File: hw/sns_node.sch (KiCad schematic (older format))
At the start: 12 parts

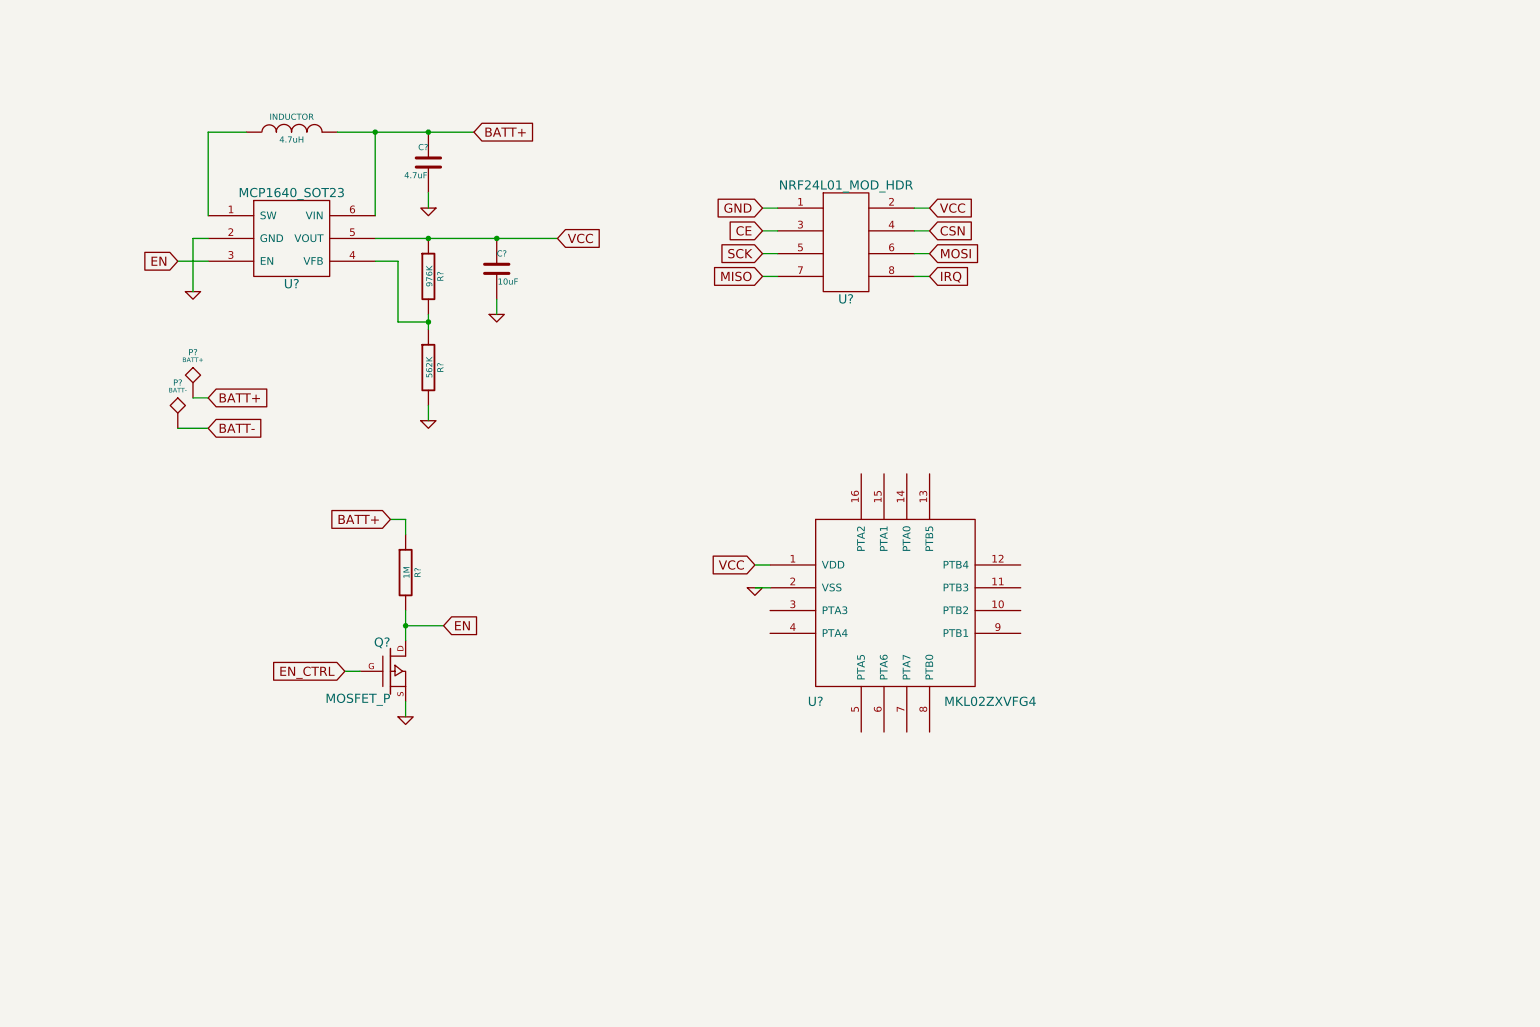
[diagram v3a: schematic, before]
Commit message: - add nrf pwr control
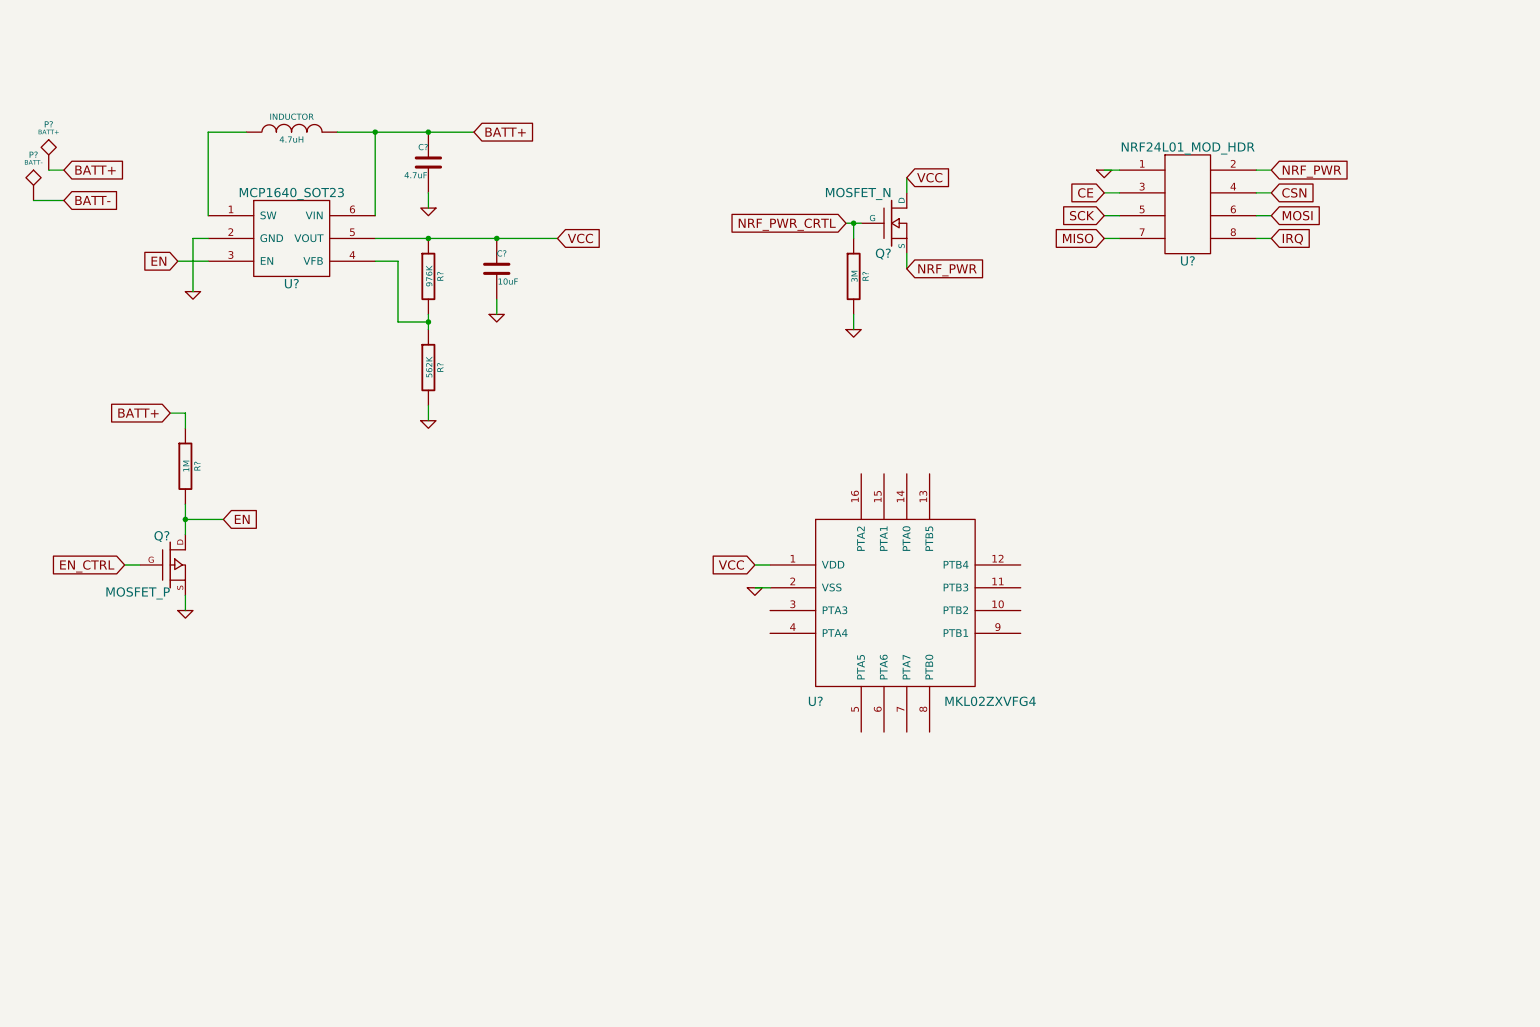
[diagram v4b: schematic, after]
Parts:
- added Q?: MOSFET_N, ~, symbol MOSFET_N
- added R?: 3M, ~, symbol R
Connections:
- net GND: now also R?.2
- net VCC: now also Q?.D; no longer U?.2
- new net NRF_PWR: Q?.S, U?.2
- new net NRF_PWR_CRTL: Q?.G, R?.1
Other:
- moved on the sheet: P?, Q?, R?, U?
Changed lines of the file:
@@
 Text GLabel 3700 1600 2    60   Input ~ 0
 BATT+
-Text GLabel 1950 3550 2    60   Input ~ 0
+Text GLabel 1000 2050 2    60   Input ~ 0
 BATT-
 $Comp
@@
 	0    -1   -1   0
 $EndComp
-Text GLabel 1950 3350 2    60   Input ~ 0
+Text GLabel 1000 1850 2    60   Input ~ 0
 BATT+
 $Comp
@@
 L TST P?
 U 1 1 5302C2B3
-P 1850 3350
-F 0 "P?" H 1850 3650 40  0000 C CNN
-F 1 "BATT+" H 1850 3600 30  0000 C CNN
-F 2 "~" H 1850 3350 60  0000 C CNN
-F 3 "~" H 1850 3350 60  0000 C CNN
-	1    1850 3350
+P 900 1850
+F 0 "P?" H 900 2150 40  0000 C CNN
+F 1 "BATT+" H 900 2100 30  0000 C CNN
+F 2 "~" H 900 1850 60  0000 C CNN
+F 3 "~" H 900 1850 60  0000 C CNN
+	1    900  1850
 	1    0    0    -1
 $EndComp
@@
 L TST P?
 U 1 1 5302C2C0
-P 1750 3550
-F 0 "P?" H 1750 3850 40  0000 C CNN
-F 1 "BATT-" H 1750 3800 30  0000 C CNN
-F 2 "~" H 1750 3550 60  0000 C CNN
-F 3 "~" H 1750 3550 60  0000 C CNN
-	1    1750 3550
-	1    0    0    -1
-$EndComp
-Wire Wire Line
-	1950 3550 1750 3550
-Wire Wire Line
-	1850 3350 1950 3350
+P 800 2050
+F 0 "P?" H 800 2350 40  0000 C CNN
+F 1 "BATT-" H 800 2300 30  0000 C CNN
+F 2 "~" H 800 2050 60  0000 C CNN
+F 3 "~" H 800 2050 60  0000 C CNN
+	1    800  2050
+	1    0    0    -1
+$EndComp
+Wire Wire Line
+	1000 2050 800  2050
+Wire Wire Line
+	900  1850 1000 1850
 Connection ~ 3050 1600
 Text GLabel 1750 2450 0    60   Input ~ 0
@@
 Wire Wire Line
 	5550 4450 5650 4450
-Text GLabel 3500 4850 2    60   Input ~ 0
+Text GLabel 2050 4150 2    60   Input ~ 0
 EN
 $Comp
 L MOSFET_P Q?
 U 1 1 5302C7F0
-P 3150 5150
-F 0 "Q?" H 3150 5340 60  0000 R CNN
-F 1 "MOSFET_P" H 3150 4970 60  0000 R CNN
-F 2 "~" H 3150 5150 60  0000 C CNN
-F 3 "~" H 3150 5150 60  0000 C CNN
-	1    3150 5150
+P 1700 4450
+F 0 "Q?" H 1700 4640 60  0000 R CNN
+F 1 "MOSFET_P" H 1700 4270 60  0000 R CNN
+F 2 "~" H 1700 4450 60  0000 C CNN
+F 3 "~" H 1700 4450 60  0000 C CNN
+	1    1700 4450
 	1    0    0    -1
 $EndComp
@@
 L R R?
 U 1 1 5302C818
-P 3250 4500
-F 0 "R?" V 3330 4500 40  0000 C CNN
-F 1 "1M" V 3257 4501 40  0000 C CNN
-F 2 "~" V 3180 4500 30  0000 C CNN
-F 3 "~" H 3250 4500 30  0000 C CNN
-	1    3250 4500
-	1    0    0    -1
-$EndComp
-Wire Wire Line
-	3500 4850 3250 4850
-Wire Wire Line
-	3250 4750 3250 4950
-Connection ~ 3250 4850
-Text GLabel 2850 5150 0    60   Input ~ 0
+P 1800 3800
+F 0 "R?" V 1880 3800 40  0000 C CNN
+F 1 "1M" V 1807 3801 40  0000 C CNN
+F 2 "~" V 1730 3800 30  0000 C CNN
+F 3 "~" H 1800 3800 30  0000 C CNN
+	1    1800 3800
+	1    0    0    -1
+$EndComp
+Wire Wire Line
+	2050 4150 1800 4150
+Wire Wire Line
+	1800 4050 1800 4250
+Connection ~ 1800 4150
+Text GLabel 1400 4450 0    60   Input ~ 0
 EN_CTRL
 Wire Wire Line
-	2950 5150 2850 5150
-Text GLabel 3150 4150 0    60   Input ~ 0
+	1500 4450 1400 4450
+Text GLabel 1700 3450 0    60   Input ~ 0
 BATT+
 Wire Wire Line
-	3150 4150 3250 4150
-Wire Wire Line
-	3250 4150 3250 4250
+	1700 3450 1800 3450
+Wire Wire Line
+	1800 3450 1800 3550
 $Comp
 L GND #PWR?
 U 1 1 5302C99C
-P 3250 5450
-F 0 "#PWR?" H 3250 5450 30  0001 C CNN
-F 1 "GND" H 3250 5380 30  0001 C CNN
-F 2 "" H 3250 5450 60  0000 C CNN
-F 3 "" H 3250 5450 60  0000 C CNN
-	1    3250 5450
-	1    0    0    -1
-$EndComp
-Wire Wire Line
-	3250 5450 3250 5350
+P 1800 4750
+F 0 "#PWR?" H 1800 4750 30  0001 C CNN
+F 1 "GND" H 1800 4680 30  0001 C CNN
+F 2 "" H 1800 4750 60  0000 C CNN
+F 3 "" H 1800 4750 60  0000 C CNN
+	1    1800 4750
+	1    0    0    -1
+$EndComp
+Wire Wire Line
+	1800 4750 1800 4650
 $Comp
 L 2X4_HDR U?
 U 1 1 53055294
-P 6150 2350
-F 0 "U?" H 6150 2000 60  0000 C CNN
-F 1 "NRF24L01_MOD_HDR" H 6150 2750 60  0000 C CNN
-F 2 "~" H 6050 2100 60  0000 C CNN
-F 3 "~" H 6050 2100 60  0000 C CNN
-	1    6150 2350
-	1    0    0    -1
-$EndComp
-Text GLabel 5600 2100 0    60   Input ~ 0
-GND
-Text GLabel 5600 2250 0    60   Input ~ 0
+P 8400 2100
+F 0 "U?" H 8400 1750 60  0000 C CNN
+F 1 "NRF24L01_MOD_HDR" H 8400 2500 60  0000 C CNN
+F 2 "~" H 8300 1850 60  0000 C CNN
+F 3 "~" H 8300 1850 60  0000 C CNN
+	1    8400 2100
+	1    0    0    -1
+$EndComp
+Text GLabel 7850 2000 0    60   Input ~ 0
 CE
-Text GLabel 5600 2400 0    60   Input ~ 0
+Text GLabel 7850 2150 0    60   Input ~ 0
 SCK
-Text GLabel 5600 2550 0    60   Input ~ 0
+Text GLabel 7850 2300 0    60   Input ~ 0
 MISO
-Text GLabel 6700 2100 2    60   Input ~ 0
+Text GLabel 8950 1850 2    60   Input ~ 0
+NRF_PWR
+Text GLabel 8950 2000 2    60   Input ~ 0
+CSN
+Text GLabel 8950 2150 2    60   Input ~ 0
+MOSI
+Text GLabel 8950 2300 2    60   Input ~ 0
+IRQ
+Wire Wire Line
+	7850 1850 7950 1850
+Wire Wire Line
+	7950 2000 7850 2000
+Wire Wire Line
+	7850 2150 7950 2150
+Wire Wire Line
+	7950 2300 7850 2300
+Wire Wire Line
+	8850 1850 8950 1850
+Wire Wire Line
+	8950 2000 8850 2000
+Wire Wire Line
+	8850 2150 8950 2150
+Wire Wire Line
+	8950 2300 8850 2300
+Text GLabel 6550 2500 2    60   Input ~ 0
+NRF_PWR
+$Comp
+L MOSFET_N Q?
+U 1 1 5305557D
+P 6450 2200
+F 0 "Q?" H 6450 2000 60  0000 R CNN
+F 1 "MOSFET_N" H 6450 2400 60  0000 R CNN
+F 2 "~" H 6450 2200 60  0000 C CNN
+F 3 "~" H 6450 2200 60  0000 C CNN
+	1    6450 2200
+	1    0    0    -1
+$EndComp
+Wire Wire Line
+	6550 1900 6550 2000
+Text GLabel 6150 2200 0    60   Input ~ 0
+NRF_PWR_CRTL
+Wire Wire Line
+	6150 2200 6250 2200
+Wire Wire Line
+	6550 2500 6550 2400
+Text GLabel 6550 1900 2    60   Input ~ 0
 VCC
-Text GLabel 6700 2250 2    60   Input ~ 0
-CSN
-Text GLabel 6700 2400 2    60   Input ~ 0
-MOSI
-Text GLabel 6700 2550 2    60   Input ~ 0
-IRQ
-Wire Wire Line
-	5600 2100 5700 2100
-Wire Wire Line
-	5700 2250 5600 2250
-Wire Wire Line
-	5600 2400 5700 2400
-Wire Wire Line
-	5700 2550 5600 2550
-Wire Wire Line
-	6600 2100 6700 2100
-Wire Wire Line
-	6700 2250 6600 2250
-Wire Wire Line
-	6600 2400 6700 2400
-Wire Wire Line
-	6700 2550 6600 2550
+$Comp
+L R R?
+U 1 1 53055831
+P 6200 2550
+F 0 "R?" V 6280 2550 40  0000 C CNN
+F 1 "3M" V 6207 2551 40  0000 C CNN
+F 2 "~" V 6130 2550 30  0000 C CNN
+F 3 "~" H 6200 2550 30  0000 C CNN
+	1    6200 2550
+	1    0    0    -1
+$EndComp
+Wire Wire Line
+	6200 2300 6200 2200
+Connection ~ 6200 2200
+$Comp
+L GND #PWR?
+U 1 1 53055869
+P 6200 2900
+F 0 "#PWR?" H 6200 2900 30  0001 C CNN
+F 1 "GND" H 6200 2830 30  0001 C CNN
+F 2 "" H 6200 2900 60  0000 C CNN
+F 3 "" H 6200 2900 60  0000 C CNN
+	1    6200 2900
+	1    0    0    -1
+$EndComp
+Wire Wire Line
+	6200 2900 6200 2800
+$Comp
+L GND #PWR?
+U 1 1 530559E5
+P 7850 1850
+F 0 "#PWR?" H 7850 1850 30  0001 C CNN
+F 1 "GND" H 7850 1780 30  0001 C CNN
+F 2 "" H 7850 1850 60  0000 C CNN
+F 3 "" H 7850 1850 60  0000 C CNN
+	1    7850 1850
+	1    0    0    -1
+$EndComp
 $EndSCHEMATC

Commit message: - add voltage sns circuit, connected to on chip comparator.
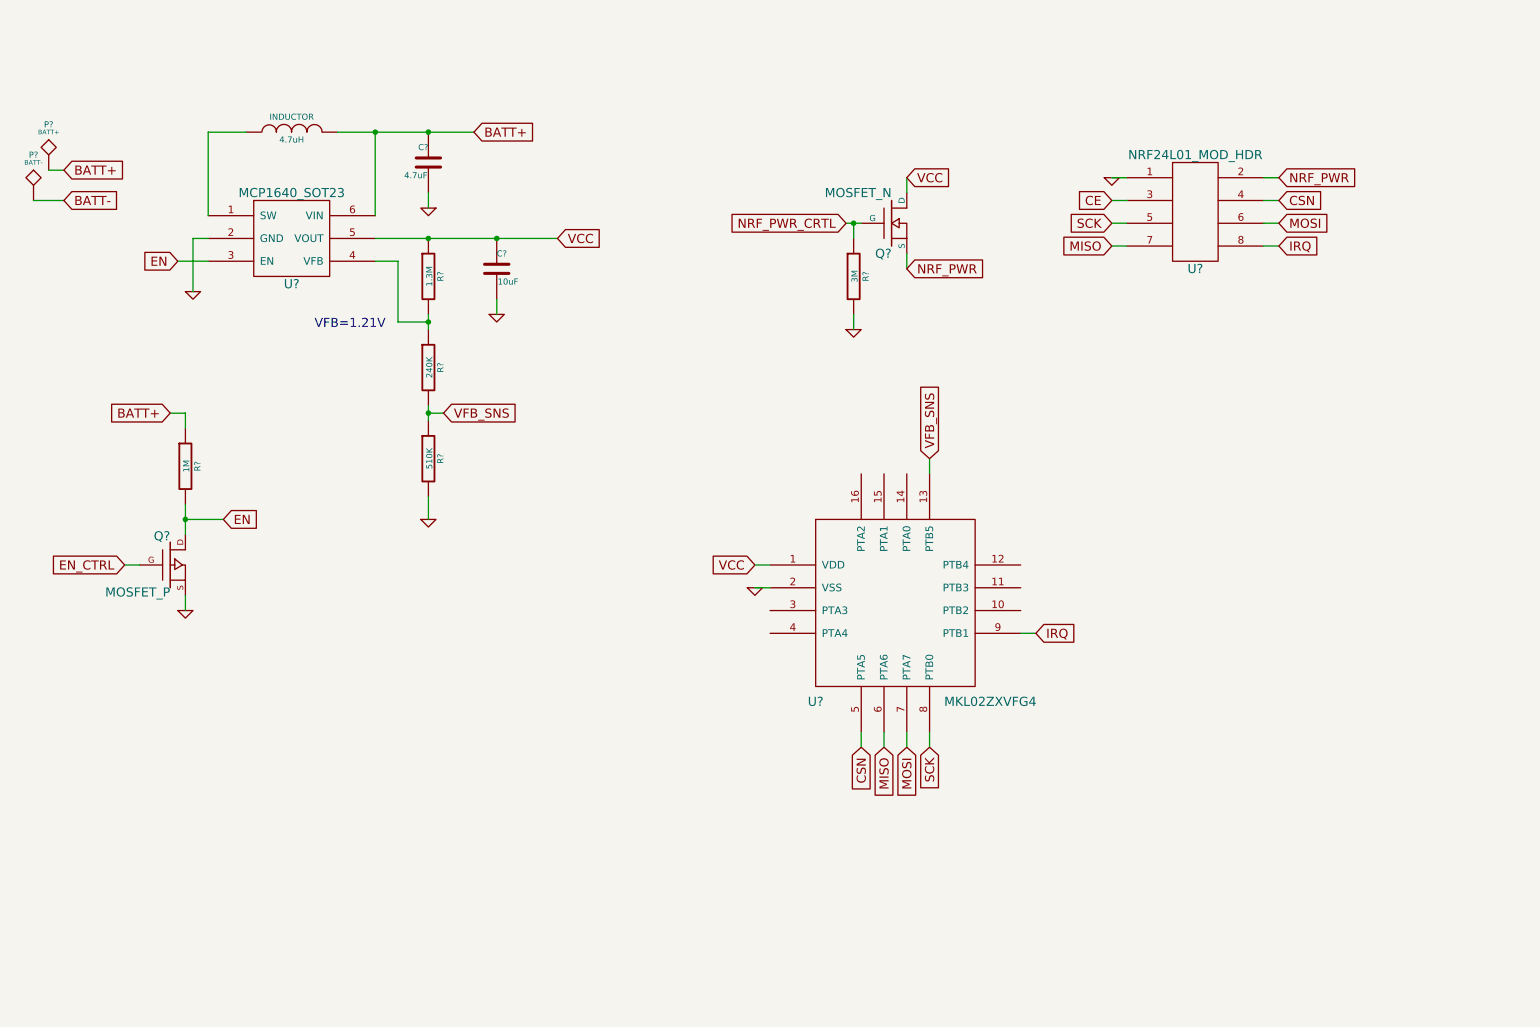
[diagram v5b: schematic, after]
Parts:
- added R?: 510K, ~, symbol R
- R?: value 976K -> 1.3M
- R?: value 562K -> 240K
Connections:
- net CSN: now also U?.5 (PTA5)
- net GND: now also R?.2; no longer R?.2
- net IRQ: now also U?.9 (PTB1)
- net MISO: now also U?.6 (PTA6)
- net MOSI: now also U?.7 (PTA7)
- net SCK: now also U?.8 (PTB0)
- net VFB_SNS: now reaches U?.13 (PTB5)
- net VFB_SNS: now also R?.2, R?.1
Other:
- note added: "VFB=1.21V"
- moved on the sheet: U?
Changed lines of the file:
@@
 P 3400 2550
 F 0 "R?" V 3480 2550 40  0000 C CNN
-F 1 "976K" V 3407 2551 40  0000 C CNN
+F 1 "1.3M" V 3407 2551 40  0000 C CNN
 F 2 "~" V 3330 2550 30  0000 C CNN
 F 3 "~" H 3400 2550 30  0000 C CNN
@@
 P 3400 3150
 F 0 "R?" V 3480 3150 40  0000 C CNN
-F 1 "562K" V 3407 3151 40  0000 C CNN
+F 1 "240K" V 3407 3151 40  0000 C CNN
 F 2 "~" V 3330 3150 30  0000 C CNN
 F 3 "~" H 3400 3150 30  0000 C CNN
@@
 L GND #PWR?
 U 1 1 5302C0E1
-P 3400 3500
-F 0 "#PWR?" H 3400 3500 30  0001 C CNN
-F 1 "GND" H 3400 3430 30  0001 C CNN
-F 2 "" H 3400 3500 60  0000 C CNN
-F 3 "" H 3400 3500 60  0000 C CNN
-	1    3400 3500
+P 3400 4150
+F 0 "#PWR?" H 3400 4150 30  0001 C CNN
+F 1 "GND" H 3400 4080 30  0001 C CNN
+F 2 "" H 3400 4150 60  0000 C CNN
+F 3 "" H 3400 4150 60  0000 C CNN
+	1    3400 4150
 	1    0    0    -1
 $EndComp
@@
 L 2X4_HDR U?
 U 1 1 53055294
-P 8400 2100
-F 0 "U?" H 8400 1750 60  0000 C CNN
-F 1 "NRF24L01_MOD_HDR" H 8400 2500 60  0000 C CNN
-F 2 "~" H 8300 1850 60  0000 C CNN
-F 3 "~" H 8300 1850 60  0000 C CNN
-	1    8400 2100
-	1    0    0    -1
-$EndComp
-Text GLabel 7850 2000 0    60   Input ~ 0
+P 8450 2150
+F 0 "U?" H 8450 1800 60  0000 C CNN
+F 1 "NRF24L01_MOD_HDR" H 8450 2550 60  0000 C CNN
+F 2 "~" H 8350 1900 60  0000 C CNN
+F 3 "~" H 8350 1900 60  0000 C CNN
+	1    8450 2150
+	1    0    0    -1
+$EndComp
+Text GLabel 7900 2050 0    60   Input ~ 0
 CE
-Text GLabel 7850 2150 0    60   Input ~ 0
+Text GLabel 7900 2200 0    60   Input ~ 0
 SCK
-Text GLabel 7850 2300 0    60   Input ~ 0
+Text GLabel 7900 2350 0    60   Input ~ 0
 MISO
-Text GLabel 8950 1850 2    60   Input ~ 0
+Text GLabel 9000 1900 2    60   Input ~ 0
 NRF_PWR
-Text GLabel 8950 2000 2    60   Input ~ 0
+Text GLabel 9000 2050 2    60   Input ~ 0
 CSN
-Text GLabel 8950 2150 2    60   Input ~ 0
+Text GLabel 9000 2200 2    60   Input ~ 0
 MOSI
-Text GLabel 8950 2300 2    60   Input ~ 0
+Text GLabel 9000 2350 2    60   Input ~ 0
 IRQ
 Wire Wire Line
-	7850 1850 7950 1850
-Wire Wire Line
-	7950 2000 7850 2000
-Wire Wire Line
-	7850 2150 7950 2150
-Wire Wire Line
-	7950 2300 7850 2300
-Wire Wire Line
-	8850 1850 8950 1850
-Wire Wire Line
-	8950 2000 8850 2000
-Wire Wire Line
-	8850 2150 8950 2150
-Wire Wire Line
-	8950 2300 8850 2300
+	7900 1900 8000 1900
+Wire Wire Line
+	8000 2050 7900 2050
+Wire Wire Line
+	7900 2200 8000 2200
+Wire Wire Line
+	8000 2350 7900 2350
+Wire Wire Line
+	8900 1900 9000 1900
+Wire Wire Line
+	9000 2050 8900 2050
+Wire Wire Line
+	8900 2200 9000 2200
+Wire Wire Line
+	9000 2350 8900 2350
 Text GLabel 6550 2500 2    60   Input ~ 0
 NRF_PWR
@@
 L GND #PWR?
 U 1 1 530559E5
-P 7850 1850
-F 0 "#PWR?" H 7850 1850 30  0001 C CNN
-F 1 "GND" H 7850 1780 30  0001 C CNN
-F 2 "" H 7850 1850 60  0000 C CNN
-F 3 "" H 7850 1850 60  0000 C CNN
-	1    7850 1850
-	1    0    0    -1
-$EndComp
+P 7900 1900
+F 0 "#PWR?" H 7900 1900 30  0001 C CNN
+F 1 "GND" H 7900 1830 30  0001 C CNN
+F 2 "" H 7900 1900 60  0000 C CNN
+F 3 "" H 7900 1900 60  0000 C CNN
+	1    7900 1900
+	1    0    0    -1
+$EndComp
+Text GLabel 6250 5650 3    60   Input ~ 0
+CSN
+Wire Wire Line
+	6250 5650 6250 5550
+Text GLabel 6400 5650 3    60   Input ~ 0
+MISO
+Wire Wire Line
+	6400 5650 6400 5550
+Text GLabel 6550 5650 3    60   Input ~ 0
+MOSI
+Wire Wire Line
+	6550 5650 6550 5550
+Text GLabel 6700 5650 3    60   Input ~ 0
+SCK
+Wire Wire Line
+	6700 5650 6700 5550
+Text GLabel 7400 4900 2    60   Input ~ 0
+IRQ
+Wire Wire Line
+	7400 4900 7300 4900
+$Comp
+L R R?
+U 1 1 530562DF
+P 3400 3750
+F 0 "R?" V 3480 3750 40  0000 C CNN
+F 1 "510K" V 3407 3751 40  0000 C CNN
+F 2 "~" V 3330 3750 30  0000 C CNN
+F 3 "~" H 3400 3750 30  0000 C CNN
+	1    3400 3750
+	1    0    0    -1
+$EndComp
+Wire Wire Line
+	3400 4000 3400 4150
+Text GLabel 3500 3450 2    60   Input ~ 0
+VFB_SNS
+Wire Wire Line
+	3500 3450 3400 3450
+Connection ~ 3400 3450
+Text Notes 2650 2900 0    60   ~ 0
+VFB=1.21V
+Text GLabel 6700 3750 1    60   Input ~ 0
+VFB_SNS
+Wire Wire Line
+	6700 3750 6700 3850
 $EndSCHEMATC
